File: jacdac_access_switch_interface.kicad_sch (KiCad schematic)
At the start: 26 parts

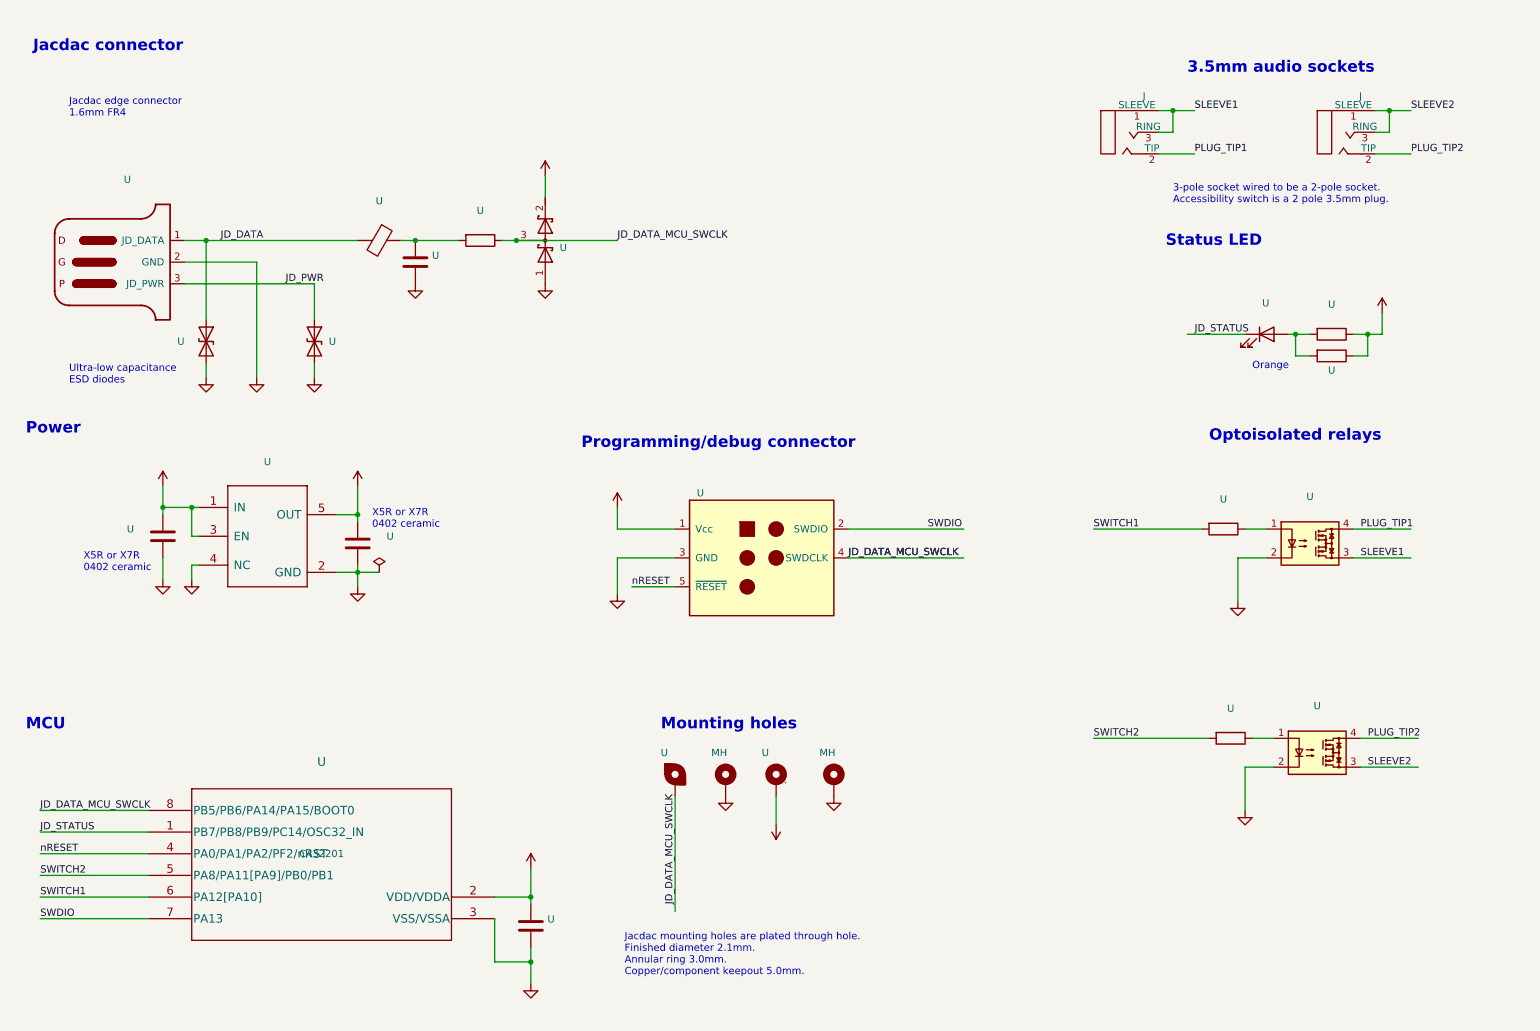
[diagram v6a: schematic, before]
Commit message: Added input protection. Changed MCU to 20 pin STM32G031F6P6
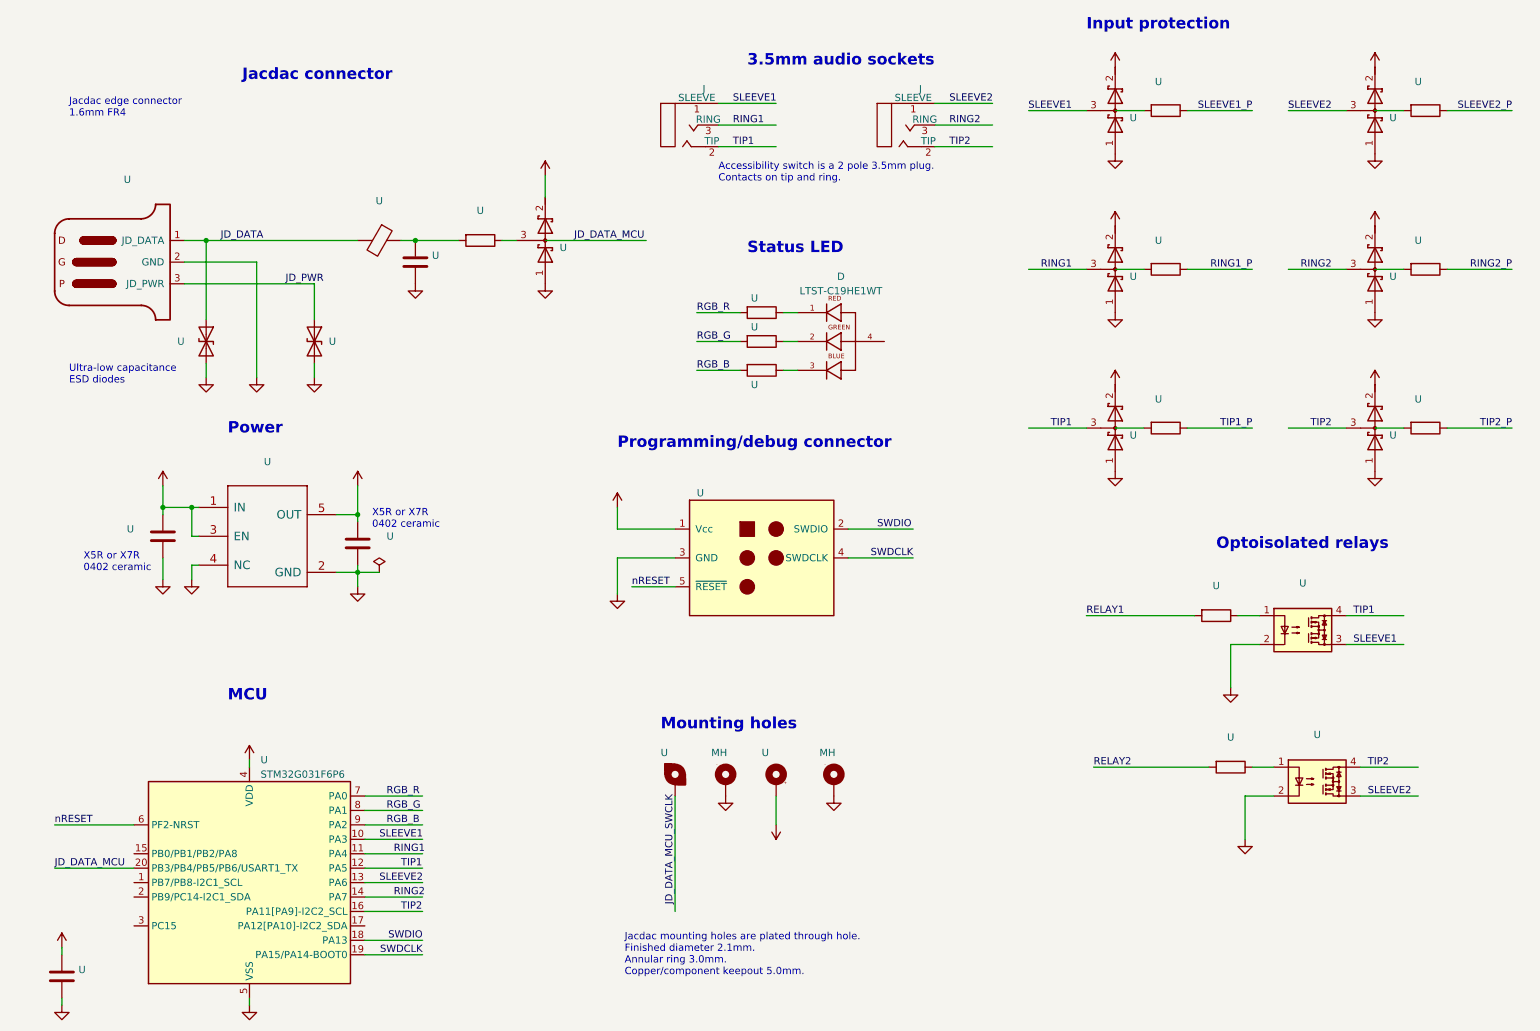
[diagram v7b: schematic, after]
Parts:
- removed U (x2): (no value), symbol Device:R
- removed U: (no value), symbol Device:LED
- removed U: (no value), symbol jacdac_access_switch_interface:STM32G031J6M6
- added D: LTST-C19HE1WT, jacdac_access_switch_interface:LED_LTST-C19HE1WT, symbol jacdac_access_switch_interface:LTST-C19HE1WT
- added U (x9): (no value), symbol Device:R
- added U (x6): (no value), symbol Device:D_Schottky_Dual_Series_AKC
- added U: STM32G031F6P6, Package_SO:TSSOP-20_4.4x6.5mm_P0.65mm, symbol jacdac_access_switch_interface:STM32G031F6P6
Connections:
- net +3V3: now also U.2 (K), U.2 (K), U.2 (K), U.2 (K), U.2 (K), U.2 (K), U.4 (VDD)
- net GND: now also U.1 (A), U.1 (A), U.1 (A), U.1 (A), U.1 (A), U.1 (A), U.5 (VSS)
- net JD_DATA_MCU_SWCLK: no longer U.1, U.3 (common), U.4 (SWDCLK)
- net SLEEVE1: now also U.10 (PA3), U.3 (common); no longer J.3 (RING)
- net SLEEVE2: now also U.13 (PA6), U.3 (common); no longer J.3 (RING)
- net SWDIO: now also U.18 (PA13)
- net nRESET: now also U.6 (PF2-NRST)
- net PLUG_TIP1 renamed TIP1
- net TIP1: now also U.12 (PA5), U.3 (common)
- net PLUG_TIP2 renamed TIP2
- net TIP2: now also U.16 (PA11[PA9]-I2C2_SCL), U.3 (common)
- net SWITCH1 renamed RELAY1
- net SWITCH2 renamed RELAY2
- new net: U.1, U.3 (common)
- new net: D.3, U.1
- new net: D.2, U.1
- new net: D.1, U.1
- new net JD_DATA_MCU: U.20 (PB3/PB4/PB5/PB6/USART1_TX)
- new net RGB_B: U.2, U.9 (PA2)
- new net RGB_G: U.2, U.8 (PA1)
- new net RGB_R: U.2, U.7 (PA0)
- new net RING1: J.3 (RING), U.11 (PA4), U.3 (common)
- new net RING1_P: U.1
- new net RING2: J.3 (RING), U.14 (PA7), U.3 (common)
- new net RING2_P: U.1
- new net SLEEVE1_P: U.1
- new net SLEEVE2_P: U.1
- new net SWDCLK: U.19 (PA15/PA14-BOOT0), U.4 (SWDCLK)
- new net TIP1_P: U.1
- new net TIP2_P: U.1
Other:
- note added: "Accessibility switch is a 2 pole 3.5mm plug. Contacts on tip and ring."
- note added: "Input protection"
- note removed: "3-pole socket wired to be a 2-pole socket. Accessibility switch is a 2 pole 3.5mm plug."
- note removed: "Orange"
- moved on the sheet: J, U

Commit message: Replaced opto-isoltated relays with discrete FET relays
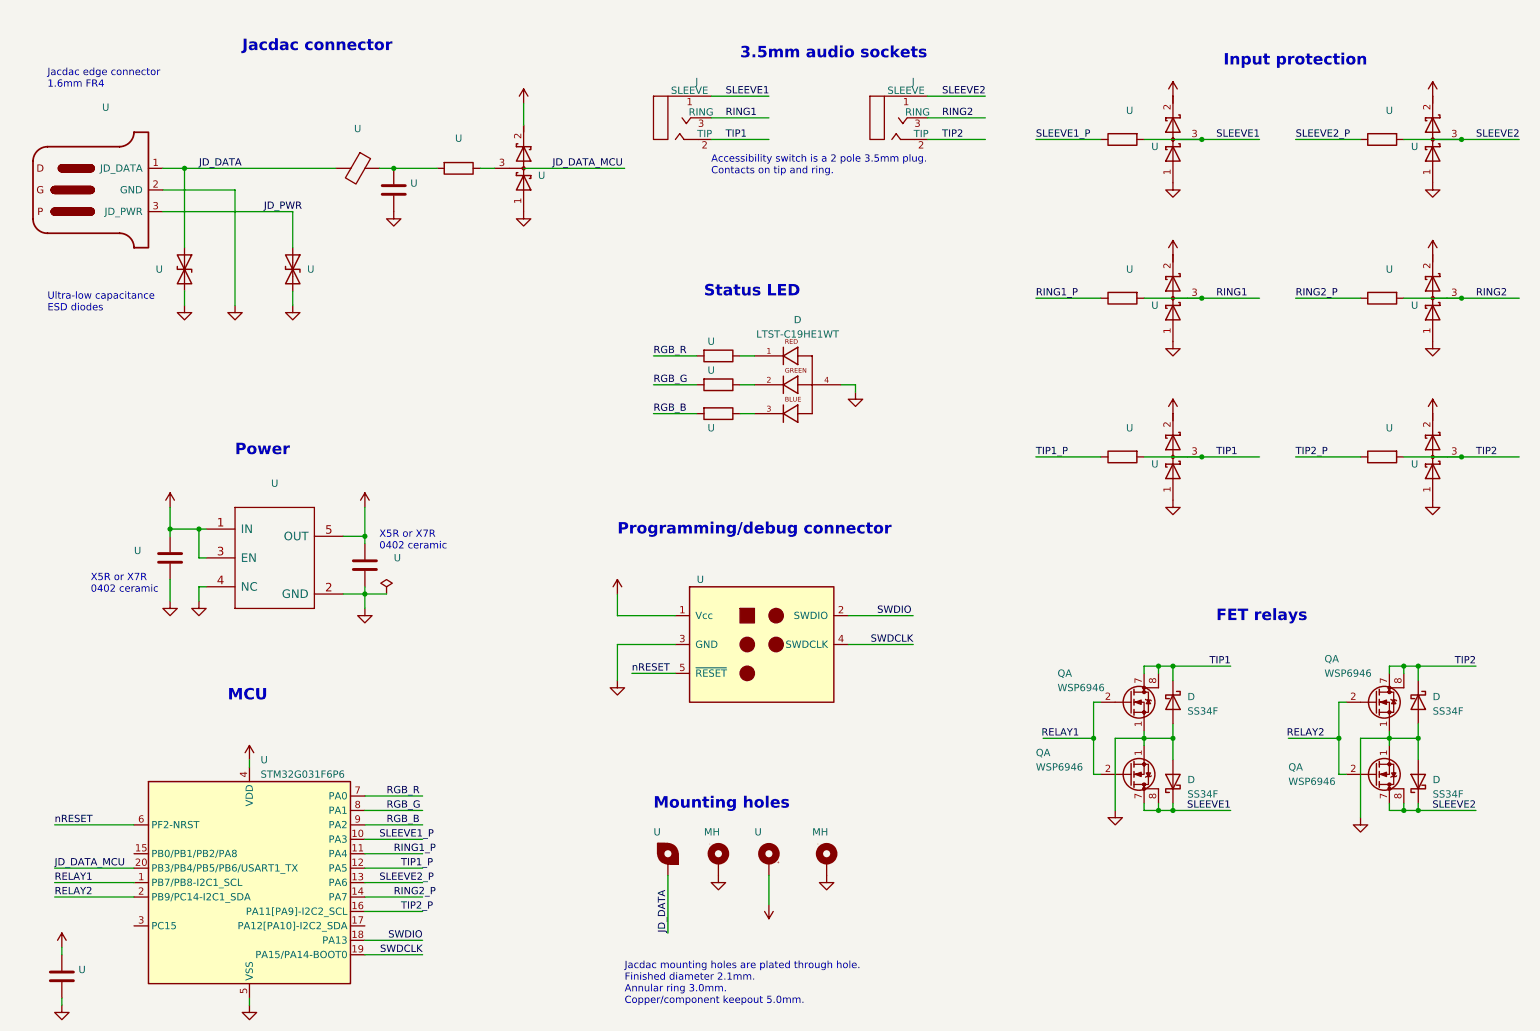
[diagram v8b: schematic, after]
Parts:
- removed U (x2): (no value), symbol jacdac_access_switch_interface:AQY282
- removed U (x2): (no value), symbol Device:R
- added D (x4): SS34F, jacdac_access_switch_interface:SMAF, symbol jacdac_access_switch_interface:SS34F
- added Q (x4): WSP6946, jacdac_access_switch_interface:SOP-8_3.9x4.9mm_P1.27mm, symbol jacdac_access_switch_interface:WSP6946
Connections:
- net JD_DATA_MCU_SWCLK is gone; now on net JD_DATA: U.MH1
- net GND: now also D.4, D.2 (A), D.2 (A), D.2 (A), D.2 (A), Q.1 (S), Q.1 (S), Q.1 (S), Q.1 (S)
- net RELAY1: now also U.1 (PB7/PB8-I2C1_SCL), Q.2 (G), Q.2 (G)
- net RELAY2: now also U.2 (PB9/PC14-I2C1_SDA), Q.2 (G), Q.2 (G)
- net RING1: now also U.2; no longer U.11 (PA4)
- net RING1_P: now also U.11 (PA4)
- net RING2: now also U.2; no longer U.14 (PA7)
- net RING2_P: now also U.14 (PA7)
- net SLEEVE1: now also U.2, D.1 (K), Q.7 (D), Q.8 (D); no longer U.10 (PA3)
- net SLEEVE1_P: now also U.10 (PA3)
- net SLEEVE2: now also U.2, D.1 (K), Q.7 (D), Q.8 (D); no longer U.13 (PA6)
- net SLEEVE2_P: now also U.13 (PA6)
- net TIP1: now also U.2, D.1 (K), Q.7 (D), Q.8 (D); no longer U.12 (PA5)
- net TIP1_P: now also U.12 (PA5)
- net TIP2: now also U.2, D.1 (K), Q.7 (D), Q.8 (D); no longer U.16 (PA11[PA9]-I2C2_SCL)
- net TIP2_P: now also U.16 (PA11[PA9]-I2C2_SCL)
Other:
- note added: "FET relays"
- note removed: "Optoisolated relays"
- moved on the sheet: D, J, MH, U
